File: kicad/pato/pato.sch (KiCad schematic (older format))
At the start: 21 parts, among them J1 DEBUG, J2 Conn_01x16, Q1 2N7002, Q2 AO3403A, U1 AMS1117-3.3, U2 ATtiny2313-20SU

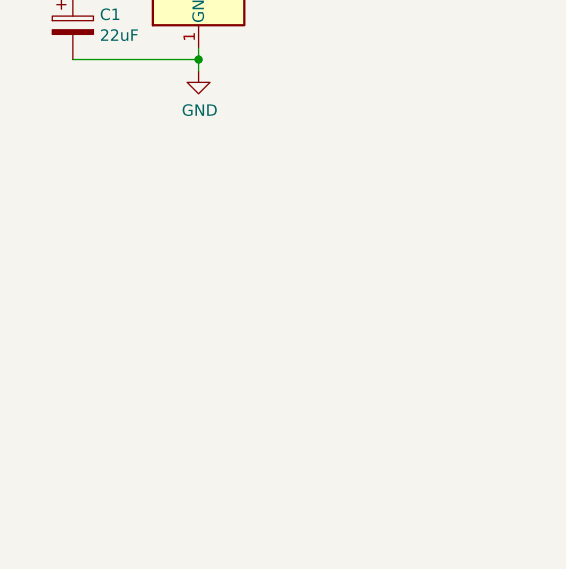
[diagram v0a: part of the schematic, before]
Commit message: Add on-board pull-up option
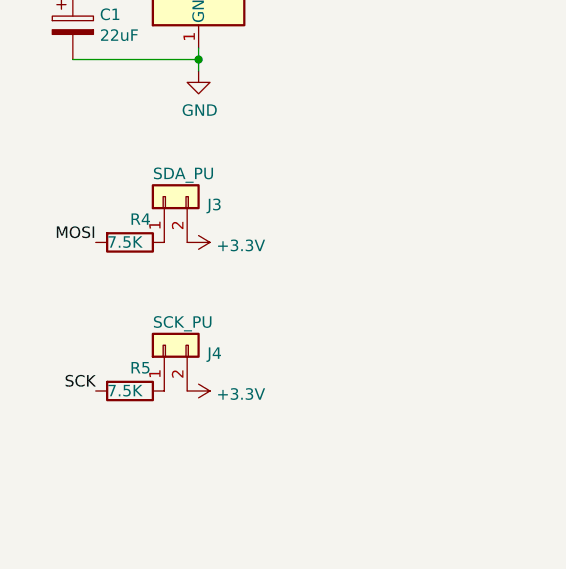
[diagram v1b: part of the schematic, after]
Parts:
- added J3: SDA_PU, Pin_Headers:Pin_Header_Straight_1x02_Pitch2.54mm, symbol Connector_Generic:Conn_01x02
- added J4: SCK_PU, Pin_Headers:Pin_Header_Straight_1x02_Pitch2.54mm, symbol Connector_Generic:Conn_01x02
- added R4, R5: 7.5K, Capacitors_SMD:C_0805_HandSoldering, symbol Device:R
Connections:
- net +3V3: now also J3.2 (Pin_2), J4.2 (Pin_2)
- net MOSI: now also R4.2
- net SCK: now also R5.2
- new net: J3.1 (Pin_1), R4.1
- new net: J4.1 (Pin_1), R5.1
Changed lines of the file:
@@
 Title "Pato: attiny2313 driver for HD44780 screens"
 Date "2021-05-18"
-Rev "20210522"
+Rev "20210531"
 Comp ""
 Comment1 "Dimitry Kloper"
@@
 Text Notes 1300 1850 0    50   ~ 0
 SCK
+$Comp
+L Device:R R4
+U 1 1 60B53465
+P 1700 4200
+F 0 "R4" V 1600 4200 50  0000 L CNN
+F 1 "7.5K" V 1700 4100 50  0000 L CNN
+F 2 "Capacitors_SMD:C_0805_HandSoldering" V 1630 4200 50  0001 C CNN
+F 3 "~" H 1700 4200 50  0001 C CNN
+	1    1700 4200
+	0    1    1    0
+$EndComp
+Text Label 1550 4200 2    50   ~ 0
+MOSI
+$Comp
+L power:+3.3V #PWR019
+U 1 1 60B563EE
+P 1950 4200
+F 0 "#PWR019" H 1950 4050 50  0001 C CNN
+F 1 "+3.3V" V 1965 4328 50  0000 L CNN
+F 2 "" H 1950 4200 50  0001 C CNN
+F 3 "" H 1950 4200 50  0001 C CNN
+	1    1950 4200
+	0    1    1    0
+$EndComp
+$Comp
+L Device:R R5
+U 1 1 60B583DC
+P 1700 4850
+F 0 "R5" V 1600 4850 50  0000 L CNN
+F 1 "7.5K" V 1700 4750 50  0000 L CNN
+F 2 "Capacitors_SMD:C_0805_HandSoldering" V 1630 4850 50  0001 C CNN
+F 3 "~" H 1700 4850 50  0001 C CNN
+	1    1700 4850
+	0    1    1    0
+$EndComp
+$Comp
+L power:+3.3V #PWR020
+U 1 1 60B586D6
+P 1950 4850
+F 0 "#PWR020" H 1950 4700 50  0001 C CNN
+F 1 "+3.3V" V 1965 4978 50  0000 L CNN
+F 2 "" H 1950 4850 50  0001 C CNN
+F 3 "" H 1950 4850 50  0001 C CNN
+	1    1950 4850
+	0    1    1    0
+$EndComp
+Text Label 1550 4850 2    50   ~ 0
+SCK
+$Comp
+L Connector_Generic:Conn_01x02 J3
+U 1 1 60B59877
+P 1850 4000
+F 0 "J3" V 1814 3812 50  0000 R CNN
+F 1 "SDA_PU" V 1950 4050 50  0000 R CNN
+F 2 "Pin_Headers:Pin_Header_Straight_1x02_Pitch2.54mm" H 1850 4000 50  0001 C CNN
+F 3 "~" H 1850 4000 50  0001 C CNN
+	1    1850 4000
+	0    -1   -1   0
+$EndComp
+$Comp
+L Connector_Generic:Conn_01x02 J4
+U 1 1 60B5C8F4
+P 1850 4650
+F 0 "J4" V 1814 4462 50  0000 R CNN
+F 1 "SCK_PU" V 1950 4700 50  0000 R CNN
+F 2 "Pin_Headers:Pin_Header_Straight_1x02_Pitch2.54mm" H 1850 4650 50  0001 C CNN
+F 3 "~" H 1850 4650 50  0001 C CNN
+	1    1850 4650
+	0    -1   -1   0
+$EndComp
 $EndSCHEMATC
